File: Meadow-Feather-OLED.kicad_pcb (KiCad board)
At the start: 2 copper layers, 74 x 23.4 mm, 23 parts, among them J1 Meadow_F7_Feather, J2 Conn_01x04

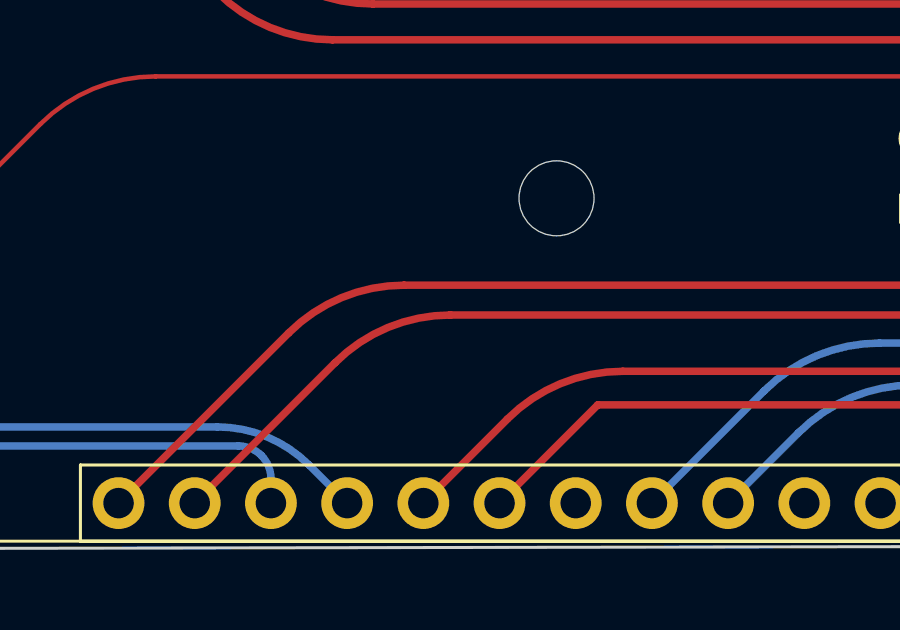
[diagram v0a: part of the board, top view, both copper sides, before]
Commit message: Fixed ERC and DRC violations.
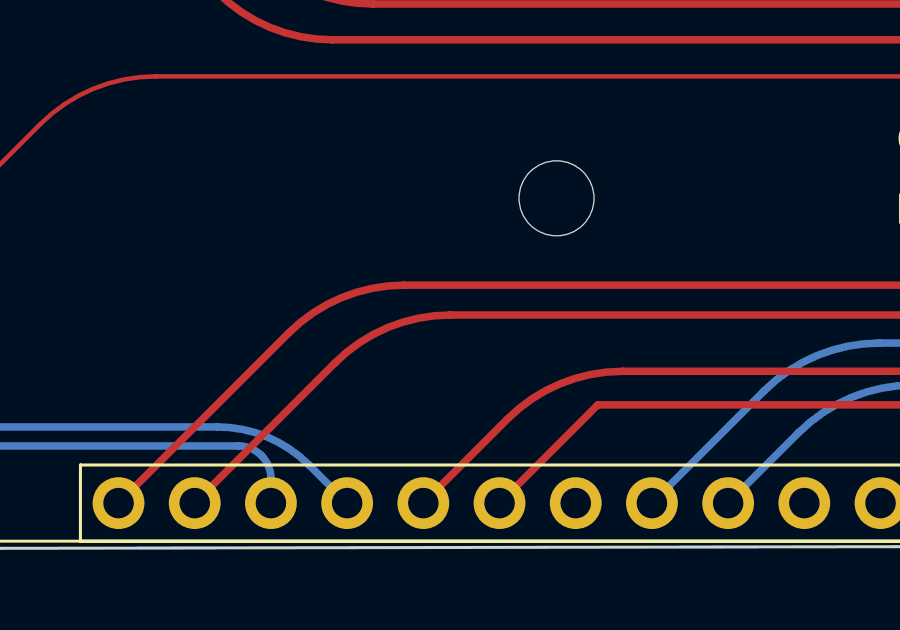
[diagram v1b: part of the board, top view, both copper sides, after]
